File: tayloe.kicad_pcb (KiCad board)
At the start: 4 copper layers, 56 x 72 mm, 91 parts, among them IC1 INA163UA_2K5, IC2 INA163UA_2K5, J1 Conn_01x11_Pin, J2 SJ3-35063B, J3 Conn_01x10_Pin, J4 Conn_01x02_Pin, J6 GSB1C41110SSHR, U1 PI3B3253LEX, U2 SN74AC74PWR, U3 FT232H, U4 AP2112K-3.3, U5 93LCxxB, U6 Si5351A-B-GT, U7 ADP7182AUJZ-5.0, Y1 830105420809, Y2 ABM8G-25.000MHZ-4Y-T3

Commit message: whatever
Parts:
- added G***: LOGO, tayloe:kity, B.Cu at (213.6, 116.8)
- added REF**: yarc, tayloe:yarc, B.Cu at (220.7, 119.0)
- moved R3 0.53 mm to (189.1, 115.3)
- moved R4 0.53 mm to (186.5, 115.3)
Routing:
- net GND: track 114.6 -> 100.1 mm
- net /Data/USB_3.3V: track 128.9 -> 122.5 mm
- net SCL: track 57.7 -> 58.7 mm
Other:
- outline, holes or cut-outs redrawn

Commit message: rev 2
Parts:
- removed G***: LOGO, tayloe:kity
- removed R12, R13, R14, R15, R22: 0, Resistor_SMD:R_1206_3216Metric_Pad1.30x1.75mm_HandSolder
- removed the REF** at (220.7, 119.0)
- added C45: 0.33u, Capacitor_SMD:C_0603_1608Metric, F.Cu at (223.9, 80.5)
- added C46: 0.1u, Capacitor_SMD:C_0603_1608Metric, F.Cu at (214.9, 80.5)
- added R23: 47k, Resistor_SMD:R_0603_1608Metric, F.Cu at (199.8, 53.8)
- added R24: 47k, Resistor_SMD:R_0603_1608Metric, F.Cu at (199.8, 65.9)
- added R25: 47k, Resistor_SMD:R_0603_1608Metric, F.Cu at (199.8, 62.8)
- added U8: L78L08_SO8, Package_SO:SOIC-8_3.9x4.9mm_P1.27mm, F.Cu at (219.4, 81.6)
- C1, C11, C15, C16, C17, C25, C26, C3, C30, C31, C32, C33, C34, C35, C36, C37, C4, C40, C43, C44, C5, C6: footprint Capacitor_SMD:C_1206_3216Metric_Pad1.33x1.80mm_HandSolder -> Capacitor_SMD:C_0603_1608Metric
- C10, C13, C2, C20, C21, C22, C23, C24, C41, C7, C8, C9: footprint Capacitor_SMD:C_1206_3216Metric_Pad1.33x1.80mm_HandSolder -> Capacitor_SMD:C_0603_1608Metric; moved to F.Cu
- C12: value 47p -> 47u
- C27, C28: value 8p -> 15p; footprint Capacitor_SMD:C_1206_3216Metric_Pad1.33x1.80mm_HandSolder -> Capacitor_SMD:C_0603_1608Metric; moved to B.Cu
- C38, C39: value 0.47u -> 0.1u; footprint Capacitor_SMD:C_1206_3216Metric_Pad1.33x1.80mm_HandSolder -> Capacitor_SMD:C_0603_1608Metric
- FB1, FB2, FB4: footprint Inductor_SMD:L_1206_3216Metric_Pad1.22x1.90mm_HandSolder -> Inductor_SMD:L_0603_1608Metric
- FB3: footprint Inductor_SMD:L_1206_3216Metric_Pad1.22x1.90mm_HandSolder -> Inductor_SMD:L_0603_1608Metric; moved to F.Cu
- IC1, IC2: value INA163UA_2K5 -> INA828IDR; footprint Package_SO:SOIC-14_3.9x8.7mm_P1.27mm -> Package_SO:SOIC-8_3.9x4.9mm_P1.27mm
- L1, L2: footprint Inductor_SMD:L_1206_3216Metric_Pad1.42x1.75mm_HandSolder -> Inductor_SMD:L_0603_1608Metric
- R1, R2: value 100 -> 330; footprint Resistor_SMD:R_1206_3216Metric_Pad1.30x1.75mm_HandSolder -> Resistor_SMD:R_0603_1608Metric
- R10, R20, R21, R3, R4: footprint Resistor_SMD:R_1206_3216Metric_Pad1.30x1.75mm_HandSolder -> Resistor_SMD:R_0603_1608Metric; moved to F.Cu
- R11, R17, R18, R19, R5, R6, R7, R8, R9: footprint Resistor_SMD:R_1206_3216Metric_Pad1.30x1.75mm_HandSolder -> Resistor_SMD:R_0603_1608Metric
- R16: value 0 -> 47k; footprint Resistor_SMD:R_1206_3216Metric_Pad1.30x1.75mm_HandSolder -> Resistor_SMD:R_0603_1608Metric
- U1: value PI3B3253LEX -> PI3B3253LE
- Y1: value 830105420809 -> ECS-120-8-36-CKM-TR3; footprint tayloe:830105420809 -> tayloe:ECS120836CKMTR3
- moved REF** 69.3 mm to (150.2, 72.8)
- moved C31 48.9 mm to (220.5, 72.3)
- moved U4 43.1 mm to (217.6, 72.2), turned to 180 degrees
- moved R4 40.5 mm to (190.7, 75.1), turned to 90 degrees
- moved R3 40.4 mm to (192.3, 75.1), turned to -90 degrees
- moved C32 36.4 mm to (214.7, 72.3)
- moved J4 32.2 mm to (224.3, 70.6), turned to 0 degrees
- moved C20 24.2 mm to (184.0, 91.2), turned to 0 degrees
- moved C39 21.4 mm to (191.4, 69.2), turned to 0 degrees
- moved FB1 19.4 mm to (182.1, 96.6), turned to 90 degrees
- moved IC1 19.3 mm to (195.1, 55.4), turned to 180 degrees
- moved C38 18.7 mm to (196.9, 73.1)
- moved FB3 18.7 mm to (181.7, 92.0), turned to 90 degrees
- moved U2 18.6 mm to (206.4, 72.5), turned to 0 degrees
- moved R21 18.6 mm to (200.0, 71.6), turned to 90 degrees
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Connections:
- C31 pad 1: VBUS -> Net-(J4-Pin_2)
- C40 pad 2: /TAYLOE_IN -> Net-(U1-YA)
- C41 pad 1: /LO_CLK -> Net-(U6-CLK0)
- C42 pad 1: Net-(J4-Pin_2) -> /AMP_Vp
- C43 pad 2: Net-(U7-EN) -> Net-(PS1-VOUT)
- C44 pad 2: Net-(U7-VOUT) -> /AMP_Vn
- C7 pad 1: VBUS -> /AMP_Vp
- C9 pad 1: VBUS -> /AMP_Vp
- FB4 pad 1: Net-(FB4-Pad1) -> Net-(U1-YA)
- IC1 pad 1: unconnected-(IC1-V_O1-Pad1) -> Net-(IC1-RG_1)
- IC1 pad 2: unconnected-(IC1-NC_1-Pad2) -> /IA0
- IC1 pad 3: /I_GS1 -> /IA3
- IC1 pad 4: /IA0 -> /AMP_Vn
- IC1 pad 5: /IA3 -> GND
- IC1 pad 6: /AMP_Vn -> Net-(IC1-OUT)
- IC1 pad 7: unconnected-(IC1-NC_2-Pad7) -> /AMP_Vp
- IC1 pad 8: Net-(IC1-SENSE) -> Net-(IC1-RG_2)
- IC2 pad 1: unconnected-(IC2-V_O1-Pad1) -> Net-(IC2-RG_1)
- IC2 pad 2: unconnected-(IC2-NC_1-Pad2) -> /IA1
- IC2 pad 3: /Q_GS1 -> /IA2
- IC2 pad 4: /IA1 -> /AMP_Vn
- IC2 pad 5: /IA2 -> GND
- IC2 pad 6: /AMP_Vn -> Net-(IC2-OUT)
- IC2 pad 7: unconnected-(IC2-NC_2-Pad7) -> /AMP_Vp
- IC2 pad 8: Net-(IC2-SENSE) -> Net-(IC2-RG_2)
- J2 pad 2: Net-(IC2-SENSE) -> Net-(IC1-OUT)
- J2 pad 3: Net-(IC1-SENSE) -> Net-(IC2-OUT)
- PS1 pad 1: Net-(PS1-(N.C.)_BOOST) -> /AMP_Vp
- PS1 pad 8: Net-(J4-Pin_2) -> /AMP_Vp
- R1 pad 1: /I_GS1 -> Net-(IC1-RG_1)
- R1 pad 2: /I_GS2 -> Net-(IC1-RG_2)
- R16 pad 1: /TAYLOE_IN -> GND
- R16 pad 2: Net-(FB4-Pad1) -> /IA0
- R2 pad 1: /Q_GS1 -> Net-(IC2-RG_1)
- R2 pad 2: /Q_GS2 -> Net-(IC2-RG_2)
- R3 pad 1: SDA -> SCL
- R3 pad 2: /Data/USB_3.3V -> /+3.3V
- R4 pad 1: /Data/USB_3.3V -> /+3.3V
- R4 pad 2: SCL -> SDA
- U1 pad 7: /TAYLOE_IN -> Net-(U1-YA)
- U1 pad 9: /TAYLOE_IN -> Net-(U1-YA)
- U4 pad 1: VBUS -> Net-(J4-Pin_2)
- U4 pad 3: VBUS -> Net-(J4-Pin_2)
- U6 pad 10: unconnected-(U6-CLK0-Pad10) -> Net-(U6-CLK0)
- U6 pad 9: /LO_CLK -> unconnected-(U6-CLK1-Pad9)
- U7 pad 2: Net-(U7-EN) -> Net-(PS1-VOUT)
- U7 pad 3: Net-(U7-EN) -> Net-(PS1-VOUT)
- U7 pad 5: Net-(U7-VOUT) -> /AMP_Vn
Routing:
- net VBUS: track 124.7 -> 23.0 mm, vias 10 -> 4
- net GND: track 100.1 -> 14.3 mm, vias 69 -> 80
- net /AMP_Vp: track 0.00 -> 78.9 mm, vias 0 -> 3
- net /Data/USB_3.3V: track 122.5 -> 88.8 mm, vias 13 -> 11
- net /AMP_Vn: track 74.4 -> 41.9 mm, vias 5 -> 3
- net /+3.3V: track 101.2 -> 72.0 mm
- net Net-(IC1-SENSE): track 26.0 -> 0.00 mm
- net SDA: track 55.7 -> 34.6 mm
- net /LO_CLK: track 15.9 -> 0.00 mm, vias 1 -> 0
- net SCL: track 58.7 -> 42.9 mm
- net /TAYLOE_IN: track 13.3 -> 0.00 mm
- net Net-(IC2-OUT): track 0.00 -> 13.1 mm
- net Net-(U1-YA): track 0.00 -> 10.8 mm
- net Net-(U7-EN): track 10.3 -> 0.00 mm
- net Net-(IC1-OUT): track 0.00 -> 8.41 mm
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- added copper zone on B.Cu, net GND
- added copper zone on F.Cu, net GND
- added copper zone on In2.Cu, net GND
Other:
- board size 56 x 72 mm -> 53 x 59.1 mm

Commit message: save
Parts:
- removed REF**: bird, tayloe:bird
- added U9: SN74CBTLV3253PWR, Package_SO:TSSOP-16_4.4x5mm_P0.65mm, F.Cu at (4.25, 2.79)
- C27, C28: moved to F.Cu
- moved C20 8.48 mm to (176.3, 87.5), turned to 180 degrees
- moved C28 7.78 mm to (184.0, 92.9), turned to 180 degrees
- moved FB3 5.07 mm to (179.4, 87.5), turned to 180 degrees
- moved C45 3.36 mm to (223.2, 77.2), turned to 180 degrees
- moved R10 2.40 mm to (181.7, 92.8), turned to 90 degrees
- moved R3 2.30 mm to (190.0, 75.0)
- moved C27 2.02 mm to (189.0, 83.6)
- moved FB2 1.53 mm to (179.4, 86.0)
- moved C18 1.18 mm to (183.8, 87.7)
- moved C42 1.09 mm to (215.6, 87.4)
- moved C46 0.95 mm to (214.9, 79.5)
- moved C29 0.95 mm to (222.3, 87.4)
- moved U8 0.95 mm to (219.4, 80.7)
- moved R4 0.82 mm to (191.5, 75.0)
- moved C14 0.39 mm to (220.1, 105.7)
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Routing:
- net /Data/USB_3.3V: track 88.8 -> 100.0 mm
- net VBUS: track 23.0 -> 28.4 mm
- net SCL: track 42.9 -> 37.7 mm
- net /Data/XCSO: track 6.94 -> 11.2 mm
- net Net-(U3-REF): track 3.40 -> 6.72 mm
- net GND: track 14.3 -> 17.5 mm, vias 80 -> 258
- net Net-(J4-Pin_2): track 18.6 -> 15.8 mm
- net /AMP_Vp: track 78.9 -> 79.8 mm
- net Net-(U3-VPLL): track 8.36 -> 7.62 mm
- net Net-(J1-Pin_10): track 15.1 -> 14.3 mm
- net SDA: track 34.6 -> 35.3 mm
- net Net-(IC2-RG_1): track 2.76 -> 2.14 mm
- net Net-(PS1-VOUT): track 22.7 -> 23.3 mm
- net Net-(IC2-RG_2): track 2.68 -> 2.15 mm
- added copper zone on F.Cu, net (none)
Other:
- outline, holes or cut-outs redrawn

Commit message: rev 3
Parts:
- removed C38, C39, C41, C46, C7, C9: 0.1u, Capacitor_SMD:C_0603_1608Metric
- removed C42: 0.1u, Capacitor_SMD:CP_Elec_5x5.3
- removed C43, C44: 4.7u, Capacitor_SMD:C_0603_1608Metric
- removed C45: 0.33u, Capacitor_SMD:C_0603_1608Metric
- removed IC1, IC2: INA828IDR, Package_SO:SOIC-8_3.9x4.9mm_P1.27mm
- removed J1: Conn_01x11_Pin, Connector_PinHeader_2.54mm:PinHeader_1x11_P2.54mm_Vertical
- removed J3: Conn_01x10_Pin, Connector_PinHeader_2.54mm:PinHeader_1x10_P2.54mm_Vertical
- removed J4: Conn_01x02_Pin, Connector_PinHeader_2.54mm:PinHeader_1x02_P2.54mm_Vertical
- removed PS1: MAX1044CPA+, tayloe:DIP794W56P254L938H457Q8N
- removed R16, R23, R24, R25: 47k, Resistor_SMD:R_0603_1608Metric
- removed R20, R21: 10k, Resistor_SMD:R_0603_1608Metric
- removed R5: 4.02k, Resistor_SMD:R_0603_1608Metric
- removed R6: 1k, Resistor_SMD:R_0603_1608Metric
- removed U8: L78L08_SO8, Package_SO:SOIC-8_3.9x4.9mm_P1.27mm
- removed U9: SN74CBTLV3253PWR, Package_SO:TSSOP-16_4.4x5mm_P0.65mm
- added FB5: 330R/0.5A, Inductor_SMD:L_0603_1608Metric, F.Cu at (197.1, 133.2)
- added G***: LOGO, tayloe:kity, F.Cu at (188.7, 149.2)
- added L3: 10u, Inductor_SMD:L_0603_1608Metric, F.Cu at (193.2, 138.6)
- added L4: 10u, Inductor_SMD:L_0603_1608Metric, F.Cu at (190.5, 131.0)
- added REF**: bird, tayloe:bird, F.Cu at (182.2, 140.3)
- added REF**: yarc, tayloe:yarc, F.Cu at (180.5, 156.5)
- C11: value 0.1u -> 22u
- C12: value 47u -> 0.47u; footprint Capacitor_SMD:CP_Elec_5x5.3 -> Capacitor_SMD:C_0603_1608Metric
- C14, C29: footprint Capacitor_SMD:CP_Elec_5x5.3 -> Capacitor_SMD:C_0603_1608Metric
- C2: value 0.1u -> 0.47u
- FB4: value 600R/0.5A -> 330R/0.5A
- R1, R2: value 330 -> 1k
- U1: value PI3B3253LE -> SN74CBTLV3253PWR
- U7: value ADP7182AUJZ-5.0 -> ADA4084-2ACPZ-R7; footprint Package_TO_SOT_SMD:TSOT-23-5 -> Package_CSP:LFCSP-8-1EP_3x3mm_P0.5mm_EP1.6x2.34mm_ThermalVias
- moved C4 82.5 mm to (197.1, 136.2), turned to -90 degrees
- moved C8 81.7 mm to (191.2, 133.3), turned to 0 degrees
- moved C15 80.0 mm to (184.6, 158.2), turned to -90 degrees
- moved C20 79.4 mm to (214.8, 156.9), turned to 0 degrees
- moved FB2 79.3 mm to (211.7, 158.4), turned to 180 degrees
- moved C3 78.6 mm to (193.4, 135.0), turned to 0 degrees
- moved C27 76.8 mm to (198.8, 159.7)
- moved FB3 76.6 mm to (211.7, 156.9), turned to 0 degrees
- moved R1 76.6 mm to (204.4, 135.1), turned to 90 degrees
- moved R18 75.7 mm to (199.2, 157.5), turned to 90 degrees
- moved R11 74.5 mm to (194.9, 158.2), turned to 0 degrees
- moved R17 74.4 mm to (187.7, 153.7), turned to 0 degrees
- moved U5 74.4 mm to (189.1, 157.1), turned to 180 degrees
- moved J2 74.2 mm to (180.3, 130.4)
- moved Y1 73.1 mm to (202.3, 158.1), turned to 180 degrees
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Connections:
- C10 pad 1: /AMP_Vn -> Net-(U7-OUT_B)
- C10 pad 2: GND -> Net-(C10-Pad2)
- C12 pad 1: Net-(C11-Pad1) -> Net-(U1-1A)
- C14 pad 1: Net-(PS1-CAP+) -> Net-(U6-VDD)
- C14 pad 2: Net-(PS1-CAP-) -> GND
- C2 pad 1: GND -> Net-(U1-VCC)
- C2 pad 2: /+3.3V -> GND
- C29 pad 1: GND -> /AMP_Vp
- C29 pad 2: Net-(PS1-VOUT) -> GND
- C31 pad 1: Net-(J4-Pin_2) -> VBUS
- C40 pad 2: Net-(U1-YA) -> Net-(U1-1A)
- C8 pad 1: /AMP_Vn -> Net-(C8-Pad1)
- C8 pad 2: GND -> Net-(U7-OUT_A)
- FB4 pad 1: Net-(U1-YA) -> Net-(C11-Pad1)
- FB4 pad 2: Net-(C11-Pad1) -> Net-(U1-1A)
- J2 pad 2: Net-(IC1-OUT) -> Net-(C10-Pad2)
- J2 pad 3: Net-(IC2-OUT) -> Net-(C8-Pad1)
- R1 pad 1: Net-(IC1-RG_1) -> /+3.3V
- R1 pad 2: Net-(IC1-RG_2) -> Net-(C11-Pad1)
- R2 pad 1: Net-(IC2-RG_1) -> GND
- R2 pad 2: Net-(IC2-RG_2) -> Net-(C11-Pad1)
- U1 pad 16: /+3.3V -> Net-(U1-VCC)
- U1 pad 7: Net-(U1-YA) -> Net-(U1-1A)
- U1 pad 9: Net-(U1-YA) -> Net-(U1-1A)
- U3 pad 15: Net-(J3-Pin_8) -> unconnected-(U3-ADBUS2-Pad15)
- U3 pad 16: Net-(J3-Pin_7) -> unconnected-(U3-ADBUS3-Pad16)
- U3 pad 17: Net-(J3-Pin_6) -> unconnected-(U3-ADBUS4-Pad17)
- U3 pad 18: Net-(J3-Pin_5) -> unconnected-(U3-ADBUS5-Pad18)
- U3 pad 19: Net-(J3-Pin_4) -> unconnected-(U3-ADBUS6-Pad19)
- U3 pad 20: Net-(J3-Pin_3) -> unconnected-(U3-ADBUS7-Pad20)
- U3 pad 21: Net-(J1-Pin_11) -> unconnected-(U3-ACBUS0-Pad21)
- U3 pad 25: Net-(J1-Pin_10) -> unconnected-(U3-ACBUS1-Pad25)
- U3 pad 26: Net-(J1-Pin_9) -> unconnected-(U3-ACBUS2-Pad26)
- U3 pad 27: Net-(J1-Pin_8) -> unconnected-(U3-ACBUS3-Pad27)
- U3 pad 28: Net-(J1-Pin_7) -> unconnected-(U3-ACBUS4-Pad28)
- U3 pad 29: Net-(J1-Pin_6) -> unconnected-(U3-ACBUS5-Pad29)
- U3 pad 30: Net-(J1-Pin_5) -> unconnected-(U3-ACBUS6-Pad30)
- U3 pad 31: Net-(J1-Pin_4) -> unconnected-(U3-ACBUS7-Pad31)
- U3 pad 32: Net-(J1-Pin_3) -> unconnected-(U3-ACBUS8-Pad32)
- U3 pad 33: Net-(J1-Pin_2) -> unconnected-(U3-ACBUS9-Pad33)
- U4 pad 1: Net-(J4-Pin_2) -> VBUS
- U4 pad 3: Net-(J4-Pin_2) -> VBUS
- U6 pad 1: /+3.3V -> Net-(U6-VDD)
- U6 pad 10: Net-(U6-CLK0) -> /CLKIN
- U6 pad 7: /+3.3V -> Net-(U6-VDD)
- U7 pad 1: GND -> Net-(U7-OUT_A)
- U7 pad 2: Net-(PS1-VOUT) -> /IA0
- U7 pad 3: Net-(PS1-VOUT) -> /IA3
- U7 pad 4: unconnected-(U7-NC-Pad4) -> GND
- U7 pad 5: /AMP_Vn -> /IA2
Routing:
- net /AMP_Vp: track 79.8 -> 3.17 mm, vias 3 -> 0
- net /AMP_Vn: track 41.9 -> 0.00 mm, vias 3 -> 0
- net /Data/USB_3.3V: track 100.0 -> 74.3 mm
- net Net-(PS1-VOUT): track 23.3 -> 0.00 mm
- net SCL: track 37.7 -> 15.3 mm, vias 2 -> 0
- net Net-(J1-Pin_2): track 21.4 -> 0.00 mm
- net SDA: track 35.3 -> 14.1 mm, vias 2 -> 0
- net Net-(J1-Pin_3): track 19.5 -> 0.00 mm
- net Net-(J1-Pin_11): track 18.9 -> 0.00 mm
- net Net-(J1-Pin_4): track 17.8 -> 0.00 mm
- net /+3.3V: track 71.5 -> 53.8 mm, vias 9 -> 10
- net Net-(J1-Pin_5): track 17.0 -> 0.00 mm
- net Net-(J1-Pin_6): track 16.1 -> 0.00 mm
- net Net-(J3-Pin_3): track 16.1 -> 0.00 mm
- net Net-(J4-Pin_2): track 15.8 -> 0.00 mm
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- removed copper zone on F.Cu, net (none)
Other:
- board size 53 x 59.1 mm -> 41.3 x 37 mm

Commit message: remove file
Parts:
- moved C32 0.81 mm to (206.1, 137.4)
- moved U4 0.81 mm to (208.9, 137.2)
- moved C31 0.75 mm to (210.9, 139.7), turned to 0 degrees
- moved C6 0.09 mm to (197.9, 127.7)
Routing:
- net GND: track 20.0 -> 31.8 mm, vias 146 -> 139
- net /IA3: track 13.3 -> 9.85 mm
- net VBUS: track 41.1 -> 40.4 mm
- net /+3.3V: track 53.8 -> 53.2 mm

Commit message: rev 3.1
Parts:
- removed REF**: bird, tayloe:bird
- removed REF**: yarc, tayloe:yarc
- added C7: 670p, Capacitor_SMD:C_0603_1608Metric, F.Cu at (192.0, 135.3)
- added C9: 670p, Capacitor_SMD:C_0603_1608Metric, F.Cu at (191.8, 127.1)
- added G**: bird, tayloe:bird, F.Cu at (182.9, 148.4)
- added R12: 100, Resistor_SMD:R_0603_1608Metric, F.Cu at (194.8, 127.2)
- added R13: 100, Resistor_SMD:R_0603_1608Metric, F.Cu at (196.3, 127.2)
- added R14: 10k, Resistor_SMD:R_0603_1608Metric, F.Cu at (192.0, 133.8)
- added R15: 10k, Resistor_SMD:R_0603_1608Metric, F.Cu at (193.3, 127.2)
- added R5: 100, Resistor_SMD:R_0603_1608Metric, F.Cu at (194.2, 134.4)
- added R6: 100, Resistor_SMD:R_0603_1608Metric, F.Cu at (195.7, 134.4)
- moved G*** 10.3 mm to (183.1, 140.5)
- moved C5 7.54 mm to (201.5, 126.6), turned to -90 degrees
- moved C10 3.64 mm to (189.6, 127.0)
- moved J2 2.64 mm to (180.4, 133.0)
- moved C3 2.37 mm to (194.8, 136.9)
- moved C8 0.96 mm to (191.4, 132.4)
- moved C29 0.87 mm to (192.2, 130.1)
- moved L4 0.87 mm to (190.7, 130.1)
- moved U7 0.87 mm to (194.7, 130.8)
- moved C6 0.50 mm to (197.8, 127.2), turned to -90 degrees
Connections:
- J2 pad 4: unconnected-(J2-Pad4) -> Net-(C8-Pad1)
- U7 pad 2: /IA0 -> Net-(U7--IN_A)
- U7 pad 3: /IA3 -> Net-(U7-+IN_A)
- U7 pad 5: /IA2 -> Net-(U7-+IN_B)
- U7 pad 6: /IA1 -> Net-(U7--IN_B)
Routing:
- net Net-(U7--IN_B): track 0.00 -> 5.15 mm
- net Net-(U7--IN_A): track 0.00 -> 4.05 mm
- net Net-(U7-OUT_B): track 1.75 -> 5.17 mm
- net Net-(U7-OUT_A): track 1.79 -> 4.95 mm
- net /IA0: track 19.1 -> 16.1 mm
- net /IA1: track 18.5 -> 16.6 mm
- net /IA2: track 14.4 -> 12.5 mm
- net Net-(U7-+IN_B): track 0.00 -> 1.72 mm
- net Net-(U7-+IN_A): track 0.00 -> 1.67 mm
- net Net-(C8-Pad1): track 5.47 -> 7.03 mm
- net Net-(C10-Pad2): track 3.62 -> 4.60 mm
- net /IA3: track 9.85 -> 10.6 mm
- net GND: track 31.8 -> 31.7 mm, vias 139 -> 59

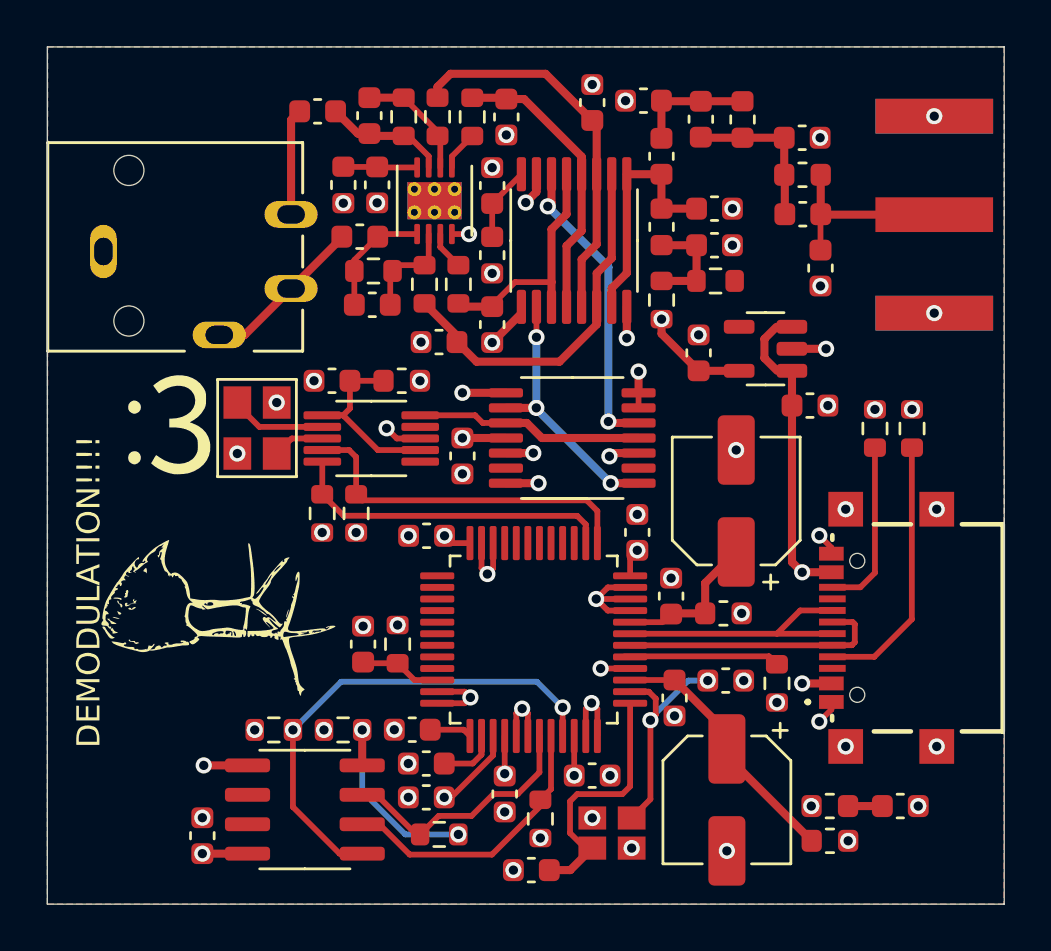
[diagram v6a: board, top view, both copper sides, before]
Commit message: i forgor via stiching (rev 3.2) (for real this time)
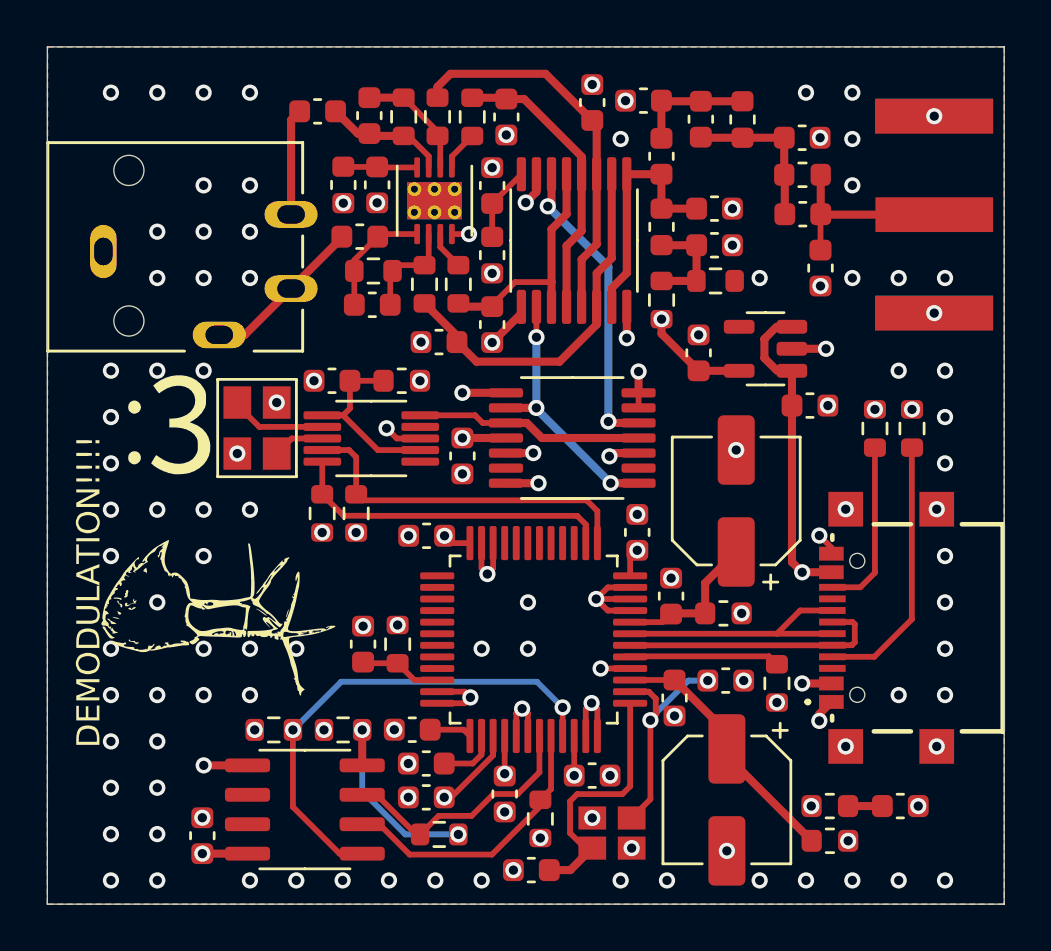
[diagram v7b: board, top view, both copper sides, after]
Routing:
- net Net-(U3-VPHY): track 12.1 -> 10.3 mm
- net /Data/EECLK: track 12.3 -> 11.3 mm
- net /Data/EEDATA: track 10.9 -> 10.2 mm
- net GND: track 31.7 -> 31.4 mm, vias 59 -> 133
